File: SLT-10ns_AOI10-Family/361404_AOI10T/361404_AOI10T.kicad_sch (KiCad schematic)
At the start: 17 parts, among them T1 T_DB, T2 T_DA, U1 12-Pin_SLx_Can

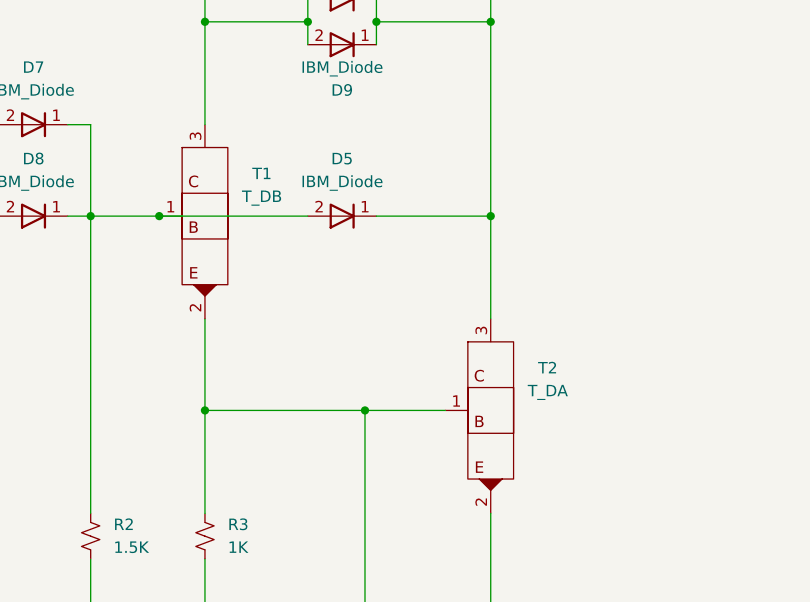
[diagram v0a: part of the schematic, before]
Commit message: Finished off the SLT-30 family of parts, started on the SLT-700 family. Changed labeling of transistors and diodes in all schematics, but have yet to update all the pdf files. This is a TODO...
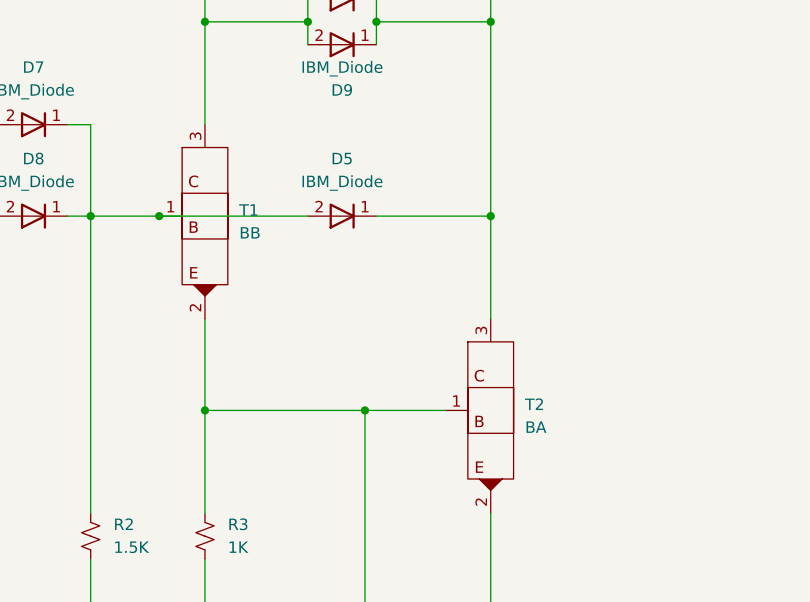
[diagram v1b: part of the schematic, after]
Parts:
- T1: value T_DB -> BB
- T2: value T_DA -> BA
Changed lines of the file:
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@@
   (symbol (lib_id "IBM_SLT-SLD:T_DB") (at 120.65 93.98 0) (unit 1)
     (in_bom yes) (on_board yes) (fields_autoplaced)
-    (property "Reference" "T1" (id 0) (at 127 89.281 0))
-    (property "Value" "T_DB" (id 1) (at 127 91.821 0))
+    (property "Reference" "T1" (id 0) (at 124.46 93.3449 0)
+      (effects (font (size 1.27 1.27)) (justify left))
+    )
+    (property "Value" "BB" (id 1) (at 124.46 95.8849 0)
+      (effects (font (size 1.27 1.27)) (justify left))
+    )
     (property "Footprint" "Package_DFN_QFN:Diodes_DFN1006-3" (id 2) (at 120.65 93.98 0)
       (effects (font (size 1.27 1.27)) hide)
@@
   (symbol (lib_id "IBM_SLT-SLD:T_DA") (at 152.4 115.57 0) (unit 1)
     (in_bom yes) (on_board yes) (fields_autoplaced)
-    (property "Reference" "T2" (id 0) (at 158.75 110.871 0))
-    (property "Value" "T_DA" (id 1) (at 158.75 113.411 0))
+    (property "Reference" "T2" (id 0) (at 156.21 114.9349 0)
+      (effects (font (size 1.27 1.27)) (justify left))
+    )
+    (property "Value" "BA" (id 1) (at 156.21 117.4749 0)
+      (effects (font (size 1.27 1.27)) (justify left))
+    )
     (property "Footprint" "Package_DFN_QFN:Diodes_DFN1006-3" (id 2) (at 152.4 115.57 0)
       (effects (font (size 1.27 1.27)) hide)
@@
     )
     (path "/95303cff-6932-4821-b7e1-1e8ef06881c6"
-      (reference "T1") (unit 1) (value "T_DB") (footprint "Package_DFN_QFN:Diodes_DFN1006-3")
+      (reference "T1") (unit 1) (value "BB") (footprint "Package_DFN_QFN:Diodes_DFN1006-3")
     )
     (path "/aca742d5-d20c-41e7-9ac8-8b36b22cfba4"
-      (reference "T2") (unit 1) (value "T_DA") (footprint "Package_DFN_QFN:Diodes_DFN1006-3")
+      (reference "T2") (unit 1) (value "BA") (footprint "Package_DFN_QFN:Diodes_DFN1006-3")
     )
     (path "/75e072b9-86c1-407b-a1c4-16b7a7044004"
